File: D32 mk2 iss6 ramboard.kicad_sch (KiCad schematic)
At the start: 34 parts, among them IC1 4116, IC2 4116, IC3 4116, IC36 4116, IC37 4116, IC38 4116, IC39 4116, IC4 4116, IC40 4116, IC41 4116, IC42 4116, IC43 4116, IC5 4116, IC6 4116, IC7 4116, IC8 4116, U1 4164, U10 4164, U11 4164, U12 4164, U13 4164, U14 4164, U15 4164, U16 4164, U2 4164, U3 4164, U4 4164, U5 4164, U6 4164, U7 4164, U8 4164, U9 4164

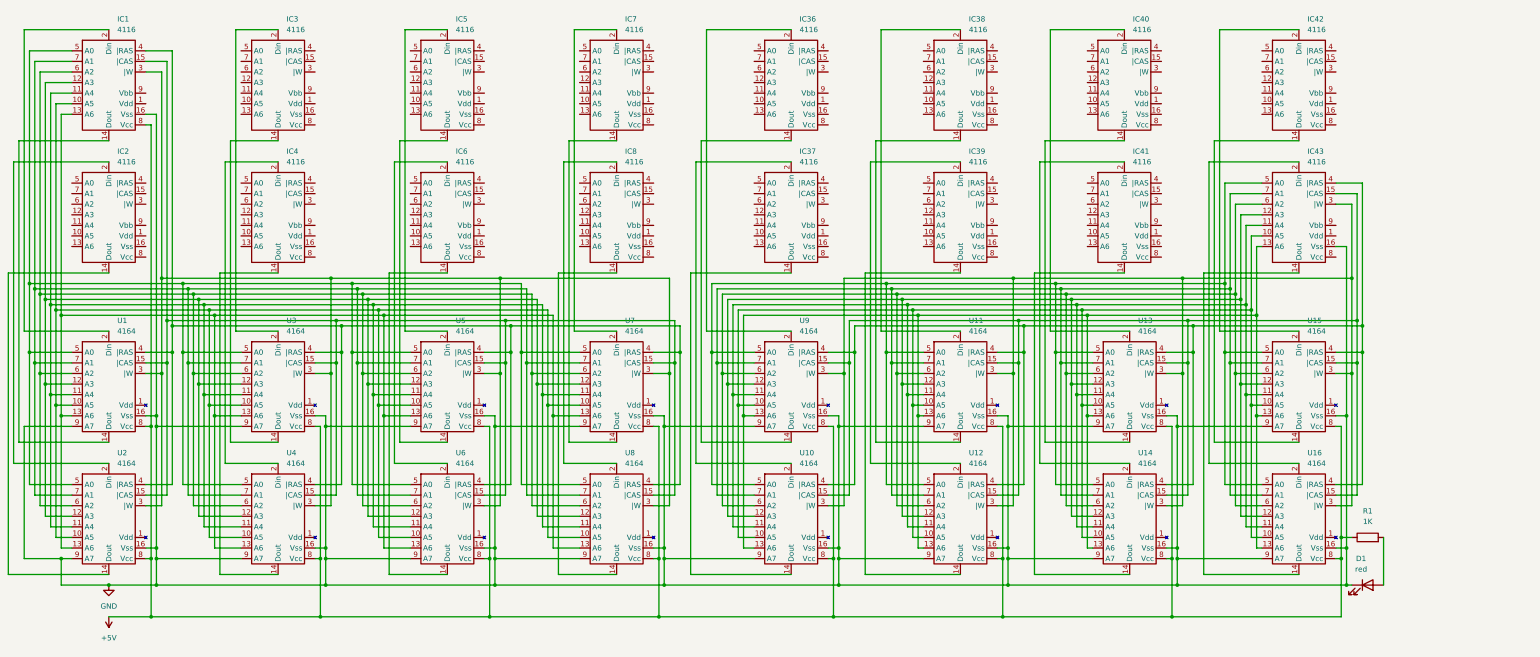
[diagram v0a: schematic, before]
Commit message: fix 4116 pin bindings
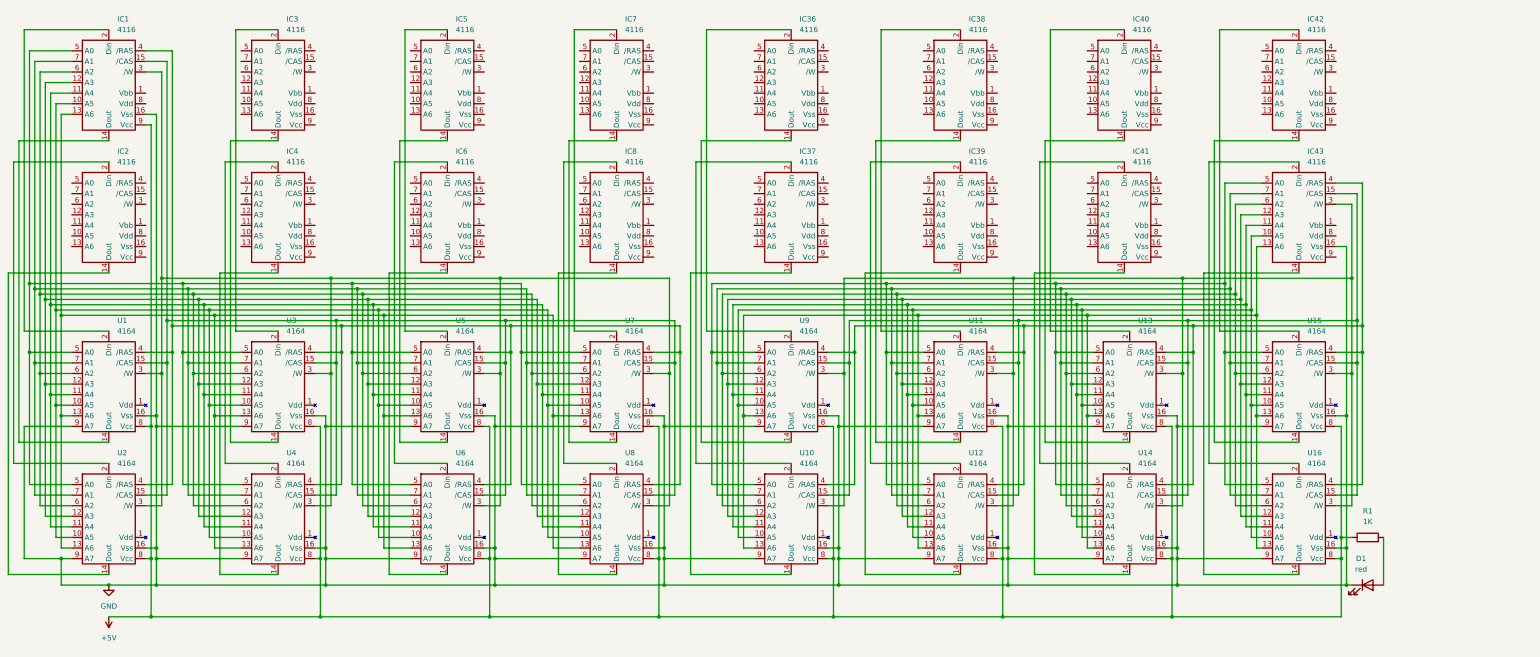
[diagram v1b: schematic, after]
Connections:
- net +5V: now also IC1.9 (Vcc); no longer IC1.8 (Vcc)
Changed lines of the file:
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@@
     (stroke (width 0) (type default) (color 0 0 0 0))
   )
-  (symbol (lib_id "4164_dram:4164") (at 186.69 161.29 0) (unit 1)
+  (symbol (lib_name "4164_11") (lib_id "4164_dram:4164") (at 186.69 161.29 0) (unit 1)
     (in_bom yes) (on_board yes) (fields_autoplaced)
     (property "Reference" "U7" (id 0) (at 188.7094 144.78 0)
@@
     (pin "9")
   )
-  (symbol (lib_id "4164_dram:4164") (at 105.41 193.04 0) (unit 1)
+  (symbol (lib_name "4164_6") (lib_id "4164_dram:4164") (at 105.41 193.04 0) (unit 1)
     (in_bom yes) (on_board yes) (fields_autoplaced)
     (property "Reference" "U4" (id 0) (at 107.4294 176.53 0)
@@
     (pin "9")
   )
-  (symbol (lib_id "4164_dram:4116") (at 350.52 120.65 0) (unit 1)
+  (symbol (lib_name "4116_13") (lib_id "4164_dram:4116") (at 350.52 120.65 0) (unit 1)
     (in_bom yes) (on_board yes) (fields_autoplaced)
     (property "Reference" "IC43" (id 0) (at 352.5394 104.14 0)
@@
     (pin "9")
   )
-  (symbol (lib_id "4164_dram:4116") (at 186.69 88.9 0) (unit 1)
+  (symbol (lib_name "4116_11") (lib_id "4164_dram:4116") (at 186.69 88.9 0) (unit 1)
     (in_bom yes) (on_board yes) (fields_autoplaced)
     (property "Reference" "IC7" (id 0) (at 188.7094 72.39 0)
@@
     (pin "9")
   )
-  (symbol (lib_id "4164_dram:4164") (at 228.6 193.04 0) (unit 1)
+  (symbol (lib_name "4164_1") (lib_id "4164_dram:4164") (at 228.6 193.04 0) (unit 1)
     (in_bom yes) (on_board yes) (fields_autoplaced)
     (property "Reference" "U10" (id 0) (at 230.6194 176.53 0)
@@
     (pin "9")
   )
-  (symbol (lib_id "4164_dram:4164") (at 350.52 193.04 0) (unit 1)
+  (symbol (lib_name "4164_14") (lib_id "4164_dram:4164") (at 350.52 193.04 0) (unit 1)
     (in_bom yes) (on_board yes) (fields_autoplaced)
     (property "Reference" "U16" (id 0) (at 352.5394 176.53 0)
@@
     (pin "9")
   )
-  (symbol (lib_id "4164_dram:4164") (at 350.52 161.29 0) (unit 1)
+  (symbol (lib_name "4164_15") (lib_id "4164_dram:4164") (at 350.52 161.29 0) (unit 1)
     (in_bom yes) (on_board yes) (fields_autoplaced)
     (property "Reference" "U15" (id 0) (at 352.5394 144.78 0)
@@
     (pin "9")
   )
-  (symbol (lib_id "4164_dram:4116") (at 228.6 120.65 0) (unit 1)
+  (symbol (lib_name "4116_1") (lib_id "4164_dram:4116") (at 228.6 120.65 0) (unit 1)
     (in_bom yes) (on_board yes) (fields_autoplaced)
     (property "Reference" "IC37" (id 0) (at 230.6194 104.14 0)
@@
     (pin "9")
   )
-  (symbol (lib_id "4164_dram:4116") (at 269.24 88.9 0) (unit 1)
+  (symbol (lib_name "4116_2") (lib_id "4164_dram:4116") (at 269.24 88.9 0) (unit 1)
     (in_bom yes) (on_board yes) (fields_autoplaced)
     (property "Reference" "IC38" (id 0) (at 271.2594 72.39 0)
@@
     (pin "9")
   )
-  (symbol (lib_id "4164_dram:4116") (at 146.05 120.65 0) (unit 1)
+  (symbol (lib_name "4116_9") (lib_id "4164_dram:4116") (at 146.05 120.65 0) (unit 1)
     (in_bom yes) (on_board yes) (fields_autoplaced)
     (property "Reference" "IC6" (id 0) (at 148.0694 104.14 0)
@@
     (pin "9")
   )
-  (symbol (lib_id "4164_dram:4116") (at 64.77 88.9 0) (unit 1)
+  (symbol (lib_name "4116_5") (lib_id "4164_dram:4116") (at 64.77 88.9 0) (unit 1)
     (in_bom yes) (on_board yes) (fields_autoplaced)
     (property "Reference" "IC1" (id 0) (at 66.7894 72.39 0)
@@
     (pin "9")
   )
-  (symbol (lib_id "4164_dram:4164") (at 186.69 193.04 0) (unit 1)
+  (symbol (lib_name "4164_12") (lib_id "4164_dram:4164") (at 186.69 193.04 0) (unit 1)
     (in_bom yes) (on_board yes) (fields_autoplaced)
     (property "Reference" "U8" (id 0) (at 188.7094 176.53 0)
@@
     (pin "9")
   )
-  (symbol (lib_id "4164_dram:4116") (at 186.69 120.65 0) (unit 1)
+  (symbol (lib_name "4116_10") (lib_id "4164_dram:4116") (at 186.69 120.65 0) (unit 1)
     (in_bom yes) (on_board yes) (fields_autoplaced)
     (property "Reference" "IC8" (id 0) (at 188.7094 104.14 0)
@@
     (pin "9")
   )
-  (symbol (lib_id "4164_dram:4164") (at 146.05 161.29 0) (unit 1)
+  (symbol (lib_name "4164_9") (lib_id "4164_dram:4164") (at 146.05 161.29 0) (unit 1)
     (in_bom yes) (on_board yes) (fields_autoplaced)
     (property "Reference" "U5" (id 0) (at 148.0694 144.78 0)
@@
     (pin "9")
   )
-  (symbol (lib_id "4164_dram:4116") (at 64.77 120.65 0) (unit 1)
+  (symbol (lib_name "4116_7") (lib_id "4164_dram:4116") (at 64.77 120.65 0) (unit 1)
     (in_bom yes) (on_board yes) (fields_autoplaced)
     (property "Reference" "IC2" (id 0) (at 66.7894 104.14 0)
@@
     (pin "1")
   )
-  (symbol (lib_id "4164_dram:4164") (at 146.05 193.04 0) (unit 1)
+  (symbol (lib_name "4164_10") (lib_id "4164_dram:4164") (at 146.05 193.04 0) (unit 1)
     (in_bom yes) (on_board yes) (fields_autoplaced)
     (property "Reference" "U6" (id 0) (at 148.0694 176.53 0)
@@
     (pin "9")
   )
-  (symbol (lib_id "4164_dram:4164") (at 64.77 193.04 0) (unit 1)
+  (symbol (lib_name "4164_5") (lib_id "4164_dram:4164") (at 64.77 193.04 0) (unit 1)
     (in_bom yes) (on_board yes) (fields_autoplaced)
     (property "Reference" "U2" (id 0) (at 66.7894 176.53 0)
@@
     (pin "9")
   )
-  (symbol (lib_id "4164_dram:4116") (at 269.24 120.65 0) (unit 1)
+  (symbol (lib_name "4116_3") (lib_id "4164_dram:4116") (at 269.24 120.65 0) (unit 1)
     (in_bom yes) (on_board yes) (fields_autoplaced)
     (property "Reference" "IC39" (id 0) (at 271.2594 104.14 0)
@@
     (pin "9")
   )
-  (symbol (lib_id "4164_dram:4116") (at 105.41 88.9 0) (unit 1)
+  (symbol (lib_name "4116_6") (lib_id "4164_dram:4116") (at 105.41 88.9 0) (unit 1)
     (in_bom yes) (on_board yes) (fields_autoplaced)
     (property "Reference" "IC3" (id 0) (at 107.4294 72.39 0)
@@
     (pin "9")
   )
-  (symbol (lib_id "4164_dram:4164") (at 105.41 161.29 0) (unit 1)
+  (symbol (lib_name "4164_8") (lib_id "4164_dram:4164") (at 105.41 161.29 0) (unit 1)
     (in_bom yes) (on_board yes) (fields_autoplaced)
     (property "Reference" "U3" (id 0) (at 107.4294 144.78 0)
@@
     (pin "9")
   )
-  (symbol (lib_id "4164_dram:4164") (at 309.88 193.04 0) (unit 1)
+  (symbol (lib_name "4164_13") (lib_id "4164_dram:4164") (at 309.88 193.04 0) (unit 1)
     (in_bom yes) (on_board yes) (fields_autoplaced)
     (property "Reference" "U14" (id 0) (at 311.8994 176.53 0)
@@
     (pin "1")
   )
-  (symbol (lib_id "4164_dram:4116") (at 146.05 88.9 0) (unit 1)
+  (symbol (lib_name "4116_12") (lib_id "4164_dram:4116") (at 146.05 88.9 0) (unit 1)
     (in_bom yes) (on_board yes) (fields_autoplaced)
     (property "Reference" "IC5" (id 0) (at 148.0694 72.39 0)
@@
     (pin "9")
   )
-  (symbol (lib_id "4164_dram:4116") (at 105.41 120.65 0) (unit 1)
+  (symbol (lib_name "4116_8") (lib_id "4164_dram:4116") (at 105.41 120.65 0) (unit 1)
     (in_bom yes) (on_board yes) (fields_autoplaced)
     (property "Reference" "IC4" (id 0) (at 107.4294 104.14 0)
@@
     (pin "2")
   )
-  (symbol (lib_id "4164_dram:4164") (at 269.24 161.29 0) (unit 1)
+  (symbol (lib_name "4164_3") (lib_id "4164_dram:4164") (at 269.24 161.29 0) (unit 1)
     (in_bom yes) (on_board yes) (fields_autoplaced)
     (property "Reference" "U11" (id 0) (at 271.2594 144.78 0)
@@
     (pin "9")
   )
-  (symbol (lib_id "4164_dram:4164") (at 269.24 193.04 0) (unit 1)
+  (symbol (lib_name "4164_4") (lib_id "4164_dram:4164") (at 269.24 193.04 0) (unit 1)
     (in_bom yes) (on_board yes) (fields_autoplaced)
     (property "Reference" "U12" (id 0) (at 271.2594 176.53 0)
@@
     (pin "9")
   )
-  (symbol (lib_id "4164_dram:4116") (at 350.52 88.9 0) (unit 1)
+  (symbol (lib_name "4116_14") (lib_id "4164_dram:4116") (at 350.52 88.9 0) (unit 1)
     (in_bom yes) (on_board yes) (fields_autoplaced)
     (property "Reference" "IC42" (id 0) (at 352.5394 72.39 0)
@@
     (pin "9")
   )
-  (symbol (lib_id "4164_dram:4116") (at 228.6 88.9 0) (unit 1)
+  (symbol (lib_name "4116_4") (lib_id "4164_dram:4116") (at 228.6 88.9 0) (unit 1)
     (in_bom yes) (on_board yes) (fields_autoplaced)
     (property "Reference" "IC36" (id 0) (at 230.6194 72.39 0)
@@
     (pin "9")
   )
-  (symbol (lib_id "4164_dram:4164") (at 64.77 161.29 0) (unit 1)
+  (symbol (lib_name "4164_7") (lib_id "4164_dram:4164") (at 64.77 161.29 0) (unit 1)
     (in_bom yes) (on_board yes) (fields_autoplaced)
     (property "Reference" "U1" (id 0) (at 66.7894 144.78 0)
@@
     (pin "9")
   )
-  (symbol (lib_id "4164_dram:4116") (at 308.61 88.9 0) (unit 1)
+  (symbol (lib_name "4116_15") (lib_id "4164_dram:4116") (at 308.61 88.9 0) (unit 1)
     (in_bom yes) (on_board yes) (fields_autoplaced)
     (property "Reference" "IC40" (id 0) (at 310.6294 72.39 0)
@@
     (pin "9")
   )
-  (symbol (lib_id "4164_dram:4164") (at 228.6 161.29 0) (unit 1)
+  (symbol (lib_name "4164_2") (lib_id "4164_dram:4164") (at 228.6 161.29 0) (unit 1)
     (in_bom yes) (on_board yes) (fields_autoplaced)
     (property "Reference" "U9" (id 0) (at 230.6194 144.78 0)

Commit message: correct 4116 pins and simplify networks
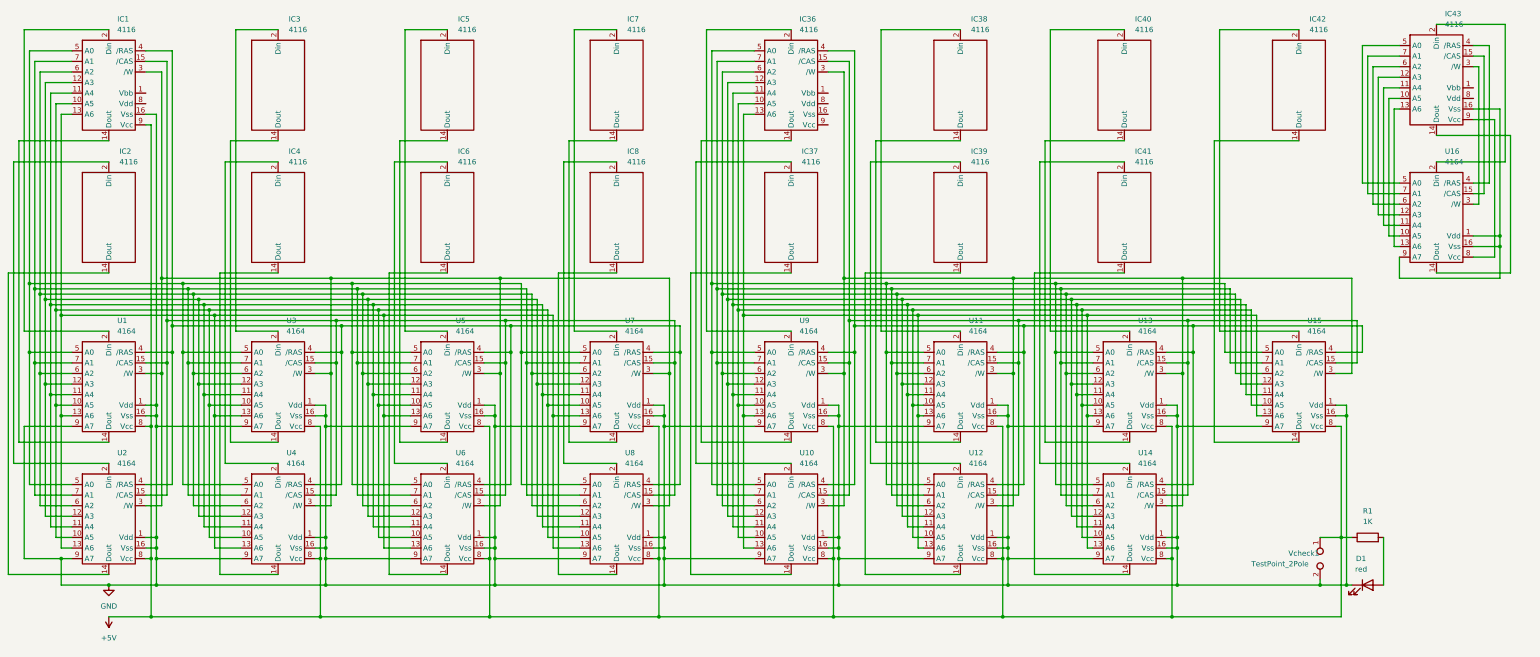
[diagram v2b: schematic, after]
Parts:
- removed IC2, IC3, IC37, IC38, IC39, IC4, IC40, IC41, IC42, IC5, IC6, IC7, IC8: 4116, Package_DIP:DIP-16_W7.62mm_Socket, symbol 4164_dram:4116
- added IC2, IC3, IC37, IC38, IC39, IC4, IC40, IC41, IC42, IC5, IC6, IC7, IC8: 4116, 4116:4116_Min_DIP-16_W7.62mm_Socket, symbol 4164_dram:4116_min
- added Vcheck1: TestPoint_2Pole, TestPoint:TestPoint_2Pads_Pitch2.54mm_Drill0.8mm, symbol Connector:TestPoint_2Pole
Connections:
- net +5V: now also Vcheck1.1; no longer U16.8 (Vcc)
- net GND: now also U1.1 (Vdd), U10.1 (Vdd), U11.1 (Vdd), U12.1 (Vdd), U13.1 (Vdd), U14.1 (Vdd), U15.1 (Vdd), U2.1 (Vdd), U3.1 (Vdd), U4.1 (Vdd), U5.1 (Vdd), U6.1 (Vdd), U7.1 (Vdd), U8.1 (Vdd), U9.1 (Vdd), Vcheck1.2; no longer IC43.16 (Vss), U16.16 (Vss), U16.9 (A7)
- net at U7.14 (Dout): now also IC7.14 (Dout)
- net at U7.2 (Din): now also IC7.2 (Din)
- net at U4.14 (Dout): now also IC4.14 (Dout)
- net at U4.2 (Din): now also IC4.2 (Din)
- net at U10.10 (A5), U11.10 (A5), U12.10 (A5)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: now also IC36.10 (A5); no longer IC43.10 (A5), U16.10 (A5)
- net at U10.11 (A4), U11.11 (A4), U12.11 (A4)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: now also IC36.11 (A4); no longer IC43.11 (A4), U16.11 (A4)
- net at U10.12 (A3), U11.12 (A3), U12.12 (A3)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: now also IC36.12 (A3); no longer IC43.12 (A3), U16.12 (A3)
- net at U10.13 (A6), U11.13 (A6), U12.13 (A6)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: now also IC36.13 (A6); no longer IC43.13 (A6), U16.13 (A6)
- net at U10.15 (/CAS), U11.15 (/CAS), U12.15 (/CAS)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: now also IC36.15 (/CAS); no longer IC43.15 (/CAS), U16.15 (/CAS)
- net at U10.3 (/W), U11.3 (/W), U12.3 (/W)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: now also IC36.3 (/W); no longer IC43.3 (/W), U16.3 (/W)
- net at U10.4 (/RAS), U11.4 (/RAS), U12.4 (/RAS)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: now also IC36.4 (/RAS); no longer IC43.4 (/RAS), U16.4 (/RAS)
- net at U10.5 (A0), U11.5 (A0), U12.5 (A0)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: now also IC36.5 (A0); no longer IC43.5 (A0), U16.5 (A0)
- net at U10.6 (A2), U11.6 (A2), U12.6 (A2)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: now also IC36.6 (A2); no longer IC43.6 (A2), U16.6 (A2)
- net at U10.7 (A1), U11.7 (A1), U12.7 (A1)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: now also IC36.7 (A1); no longer IC43.7 (A1), U16.7 (A1)
- net at IC43.9 (Vcc): now also U16.8 (Vcc)
- net at U10.14 (Dout): now also IC37.14 (Dout)
- net at U10.2 (Din): now also IC37.2 (Din)
- net at U16.1 (Vdd): now also IC43.16 (Vss), U16.16 (Vss), U16.9 (A7)
- net at U15.14 (Dout): now also IC42.14 (Dout)
- net at U15.2 (Din): now also IC42.2 (Din)
- net at U11.14 (Dout): now also IC38.14 (Dout)
- net at U11.2 (Din): now also IC38.2 (Din)
- net at U6.14 (Dout): now also IC6.14 (Dout)
- net at U6.2 (Din): now also IC6.2 (Din)
- net at U8.14 (Dout): now also IC8.14 (Dout)
- net at U8.2 (Din): now also IC8.2 (Din)
- net at U5.14 (Dout): now also IC5.14 (Dout)
- net at U5.2 (Din): now also IC5.2 (Din)
- net at U2.14 (Dout): now also IC2.14 (Dout)
- net at U2.2 (Din): now also IC2.2 (Din)
- net at U12.14 (Dout): now also IC39.14 (Dout)
- net at U12.2 (Din): now also IC39.2 (Din)
- net at U3.14 (Dout): now also IC3.14 (Dout)
- net at U3.2 (Din): now also IC3.2 (Din)
- net at U14.14 (Dout): now also IC41.14 (Dout)
- net at U14.2 (Din): now also IC41.2 (Din)
- net at U13.14 (Dout): now also IC40.14 (Dout)
- net at U13.2 (Din): now also IC40.2 (Din)
- new net: IC43.10 (A5), U16.10 (A5)
- new net: IC43.11 (A4), U16.11 (A4)
- new net: IC43.12 (A3), U16.12 (A3)
- new net: IC43.13 (A6), U16.13 (A6)
- new net: IC43.15 (/CAS), U16.15 (/CAS)
- new net: IC43.3 (/W), U16.3 (/W)
- new net: IC43.4 (/RAS), U16.4 (/RAS)
- new net: IC43.5 (A0), U16.5 (A0)
- new net: IC43.6 (A2), U16.6 (A2)
- new net: IC43.7 (A1), U16.7 (A1)
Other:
- moved on the sheet: IC43

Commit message: make A8 configurable on each bank
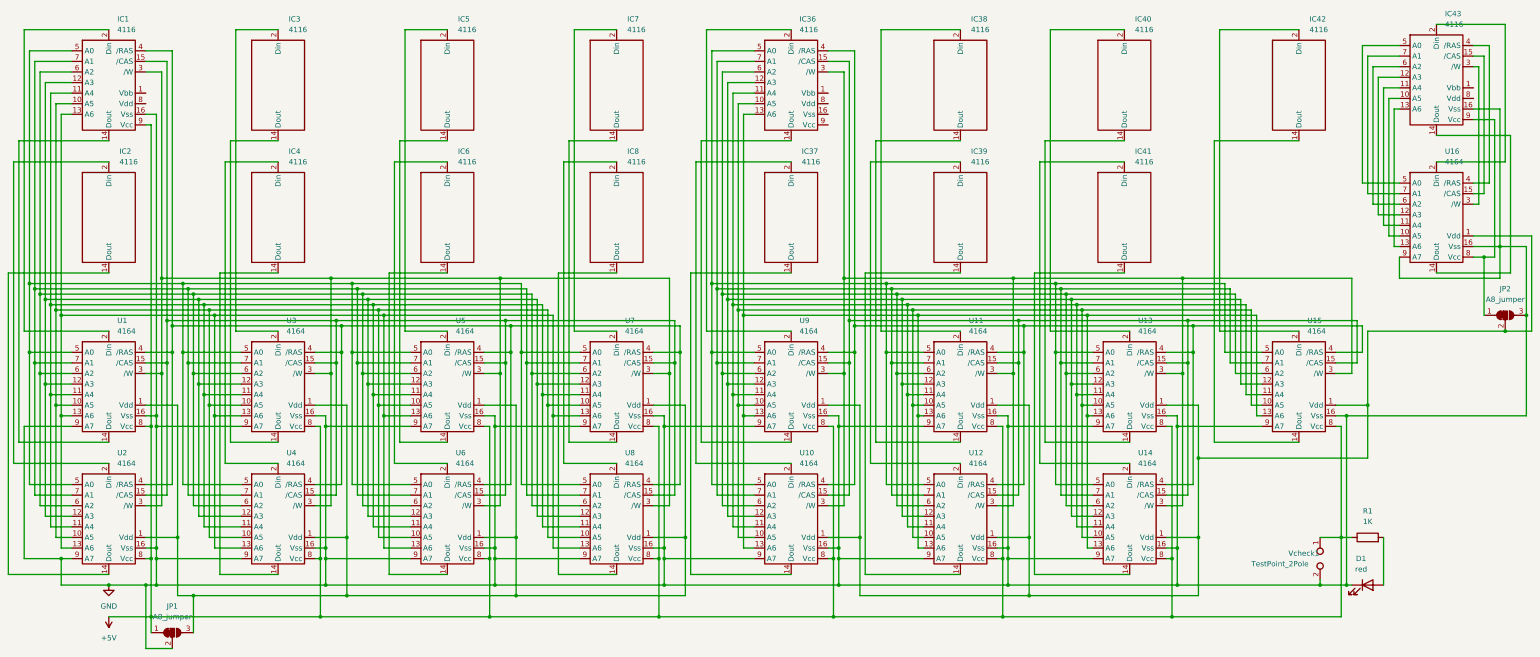
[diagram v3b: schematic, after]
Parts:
- added JP1, JP2: A8_jumper, Jumper:SolderJumper-3_P1.3mm_Bridged2Bar12_RoundedPad1.0x1.5mm, symbol 4164_dram:A8_jumper
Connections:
- net +5V: now also JP1.1 (A)
- net GND: now also IC43.16 (Vss), U16.16 (Vss), U16.9 (A7), JP1.2 (C), JP2.3 (B); no longer U1.1 (Vdd), U10.1 (Vdd), U11.1 (Vdd), U12.1 (Vdd), U13.1 (Vdd), U14.1 (Vdd), U15.1 (Vdd), U2.1 (Vdd), U3.1 (Vdd), U4.1 (Vdd), U5.1 (Vdd), U6.1 (Vdd), U7.1 (Vdd), U8.1 (Vdd), U9.1 (Vdd)
- net at IC43.9 (Vcc), U16.8 (Vcc): now also JP2.1 (A)
- new net: JP1.3 (B), U1.1 (Vdd), U2.1 (Vdd), U3.1 (Vdd), U4.1 (Vdd), U5.1 (Vdd), U6.1 (Vdd), U7.1 (Vdd), U8.1 (Vdd)
- new net: JP2.2 (C), U10.1 (Vdd), U11.1 (Vdd), U12.1 (Vdd), U13.1 (Vdd), U14.1 (Vdd), U15.1 (Vdd), U16.1 (Vdd), U9.1 (Vdd)
